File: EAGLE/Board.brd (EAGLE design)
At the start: 100 x 70 mm, 168 parts, among them J1 JUMPER_SOLDER_1X2, J10 JUMPER_SOLDER_1X2, J11 JUMPER_SOLDER_1X2, J12 KF301-2P, J2 JUMPER_SOLDER_1X2, J3 JUMPER_SOLDER_1X2, J4 JUMPER_SOLDER_1X2, J5 JUMPER_SOLDER_1X2, J6 JUMPER_SOLDER_1X2, J8 KF301-2P, J9 JUMPER_SOLDER_1X2, Q1 500mA/300V, Q2 500mA/300V, Q3 FDN337N, U1 SN74HC04PW, U2 ESP32-WROOM-32, U3 CH340C, U4 AMS1117, U6 PCA9635PW, U7 SN74HC04PW, U8 SN74HC04PW, U9 LTC1694IS5#TRPBF, X1 JST-XH-04-PIN-LONG-PAD, X2 JST-XH-04-PIN-LONG-PAD, X3 JST-XH-02-PIN-LONG-PAD

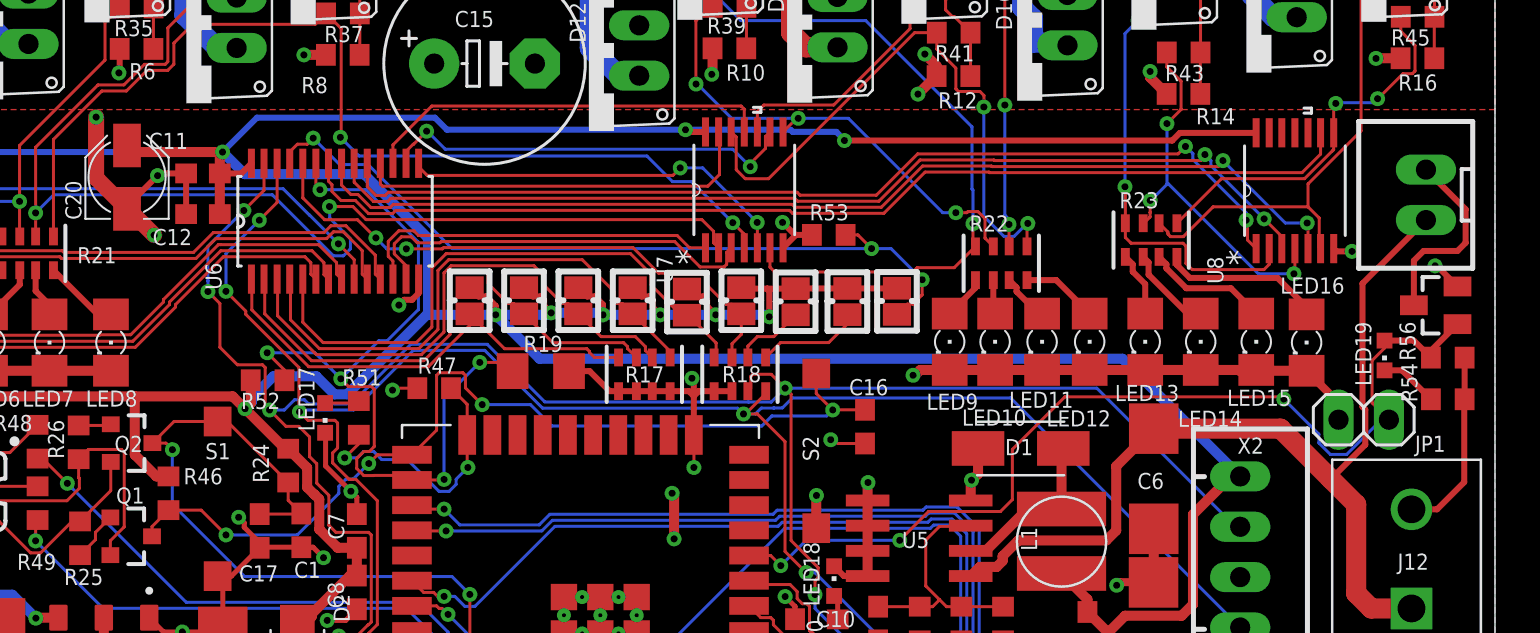
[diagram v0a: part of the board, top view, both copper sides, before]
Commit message: Update EAGLE files to latest version
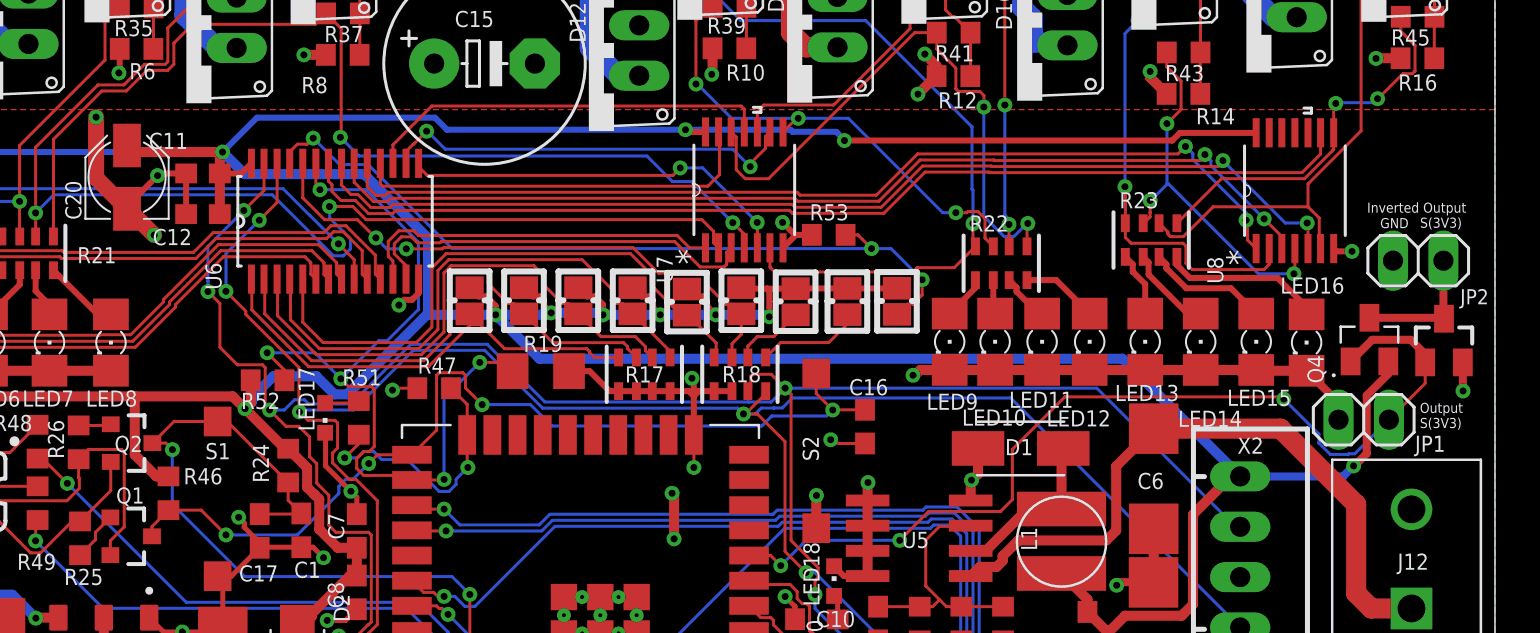
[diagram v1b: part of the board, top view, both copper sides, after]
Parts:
- removed LED19: (no value), dp_devices:LED-603
- removed R54, R56: 10K, rcl:R0603
- removed X3: JST-XH-02-PIN-LONG-PAD, Rembrandt Electronics - JST XH Connectors v1-0:JST-XH-02-PACKAGE-LONG-PAD
- added JP2: (no value), pinhead:1X02
- added Q4: FDN340P, FDN340P:SOT95P240X120-3N
- moved Q3 1.83 mm to (97.4, 23.9), turned to 0 degrees
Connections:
- removed net N$83: LED19.C, R54.2
- net +3V3: now also Q4.2
- net GND: now also JP2.2; no longer R54.1, R56.1
- net N$37: now also JP2.1, Q4.3; no longer X3.2
- net SOLENOIDS_ON: now also Q4.1; no longer LED19.A, R56.2
- net VDD: no longer X3.1
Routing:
- net VDD: track 48.9 -> 33.7 mm
- net +3V3: track 335.0 -> 347.0 mm, vias 13 -> 14
- net GND: track 205.3 -> 195.0 mm
- net N$37: track 9.75 -> 6.72 mm
- net N$83: track 2.94 -> 0.00 mm
- net SOLENOIDS_ON: track 49.2 -> 48.3 mm
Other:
- board text added: "GND"
- board text added: "Inverted Output"
- board text added: "Output S(3V3)"
- board text added: "S(3V3)"
